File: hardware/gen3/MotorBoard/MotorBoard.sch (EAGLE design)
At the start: 249 parts, among them M10O1 TEST_PT, M1O2 TEST_PT, M1O3 TEST_PT, M2O1 TEST_PT, M2O2 TEST_PT, M2O3 TEST_PT, M3O1 TEST_PT, M3O2 TEST_PT, M3O3 TEST_PT, M4O1 TEST_PT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

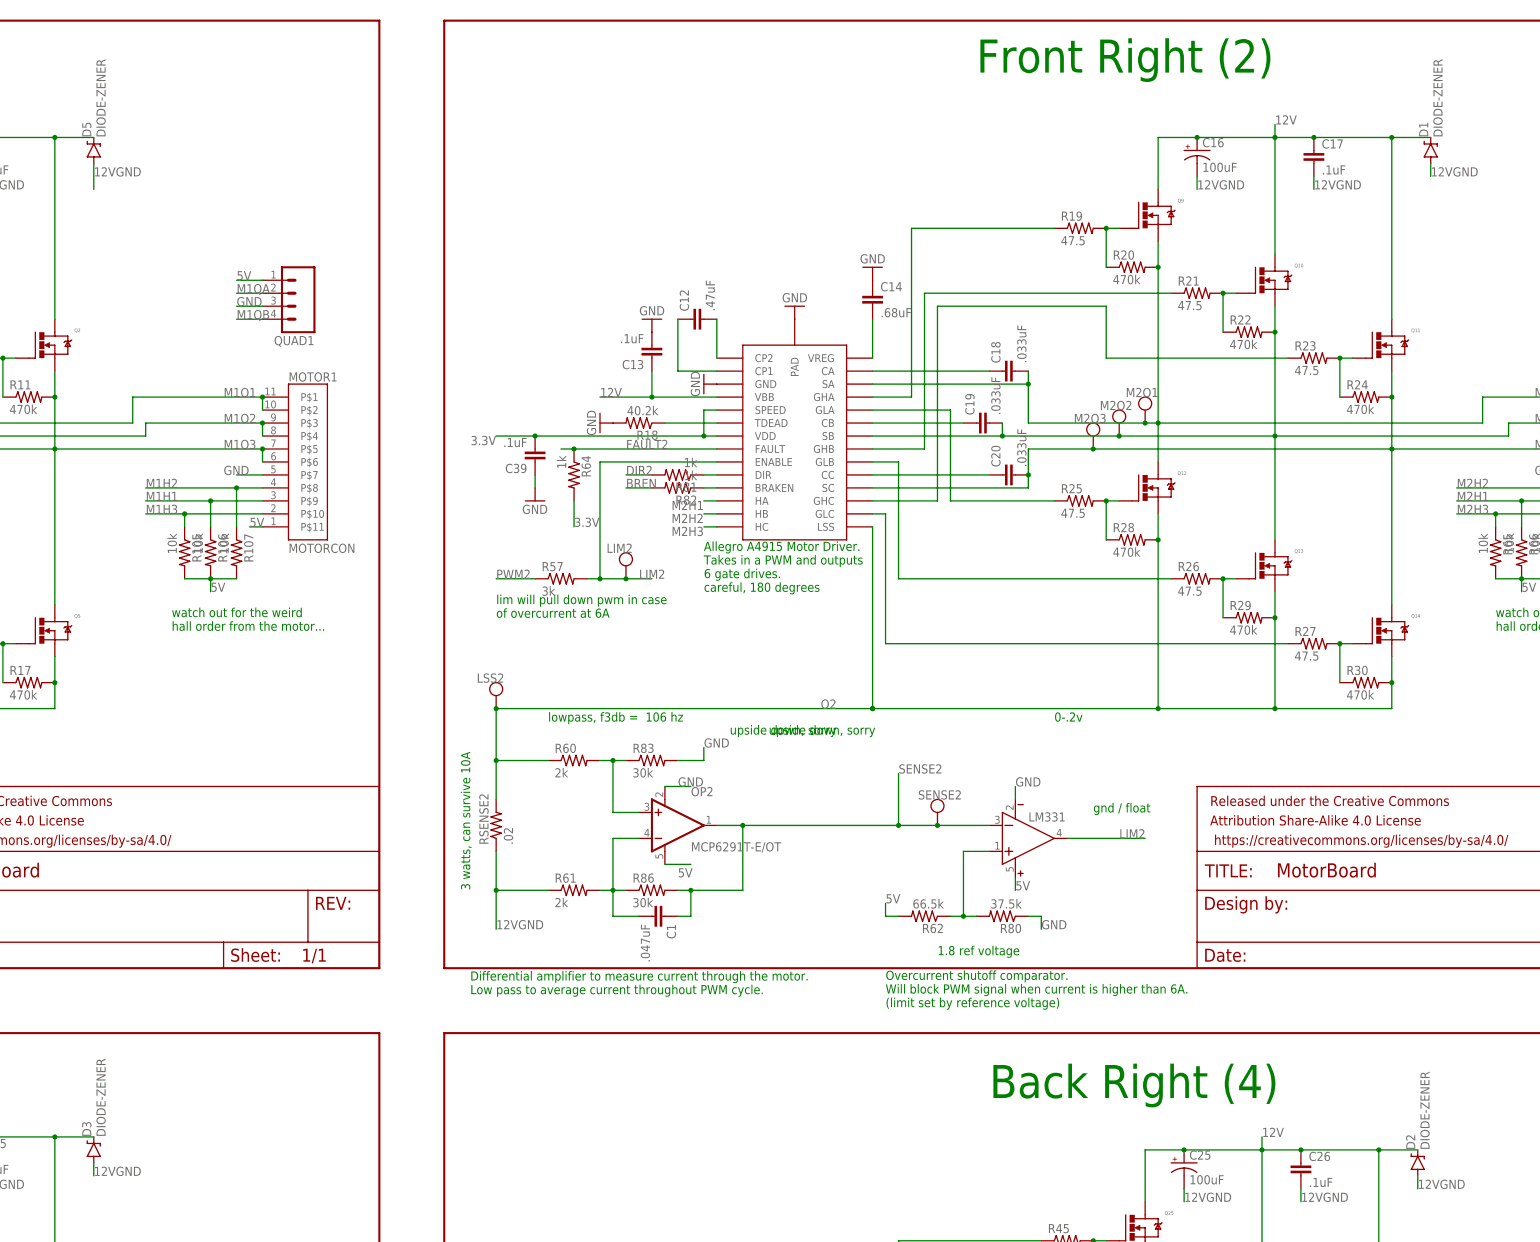
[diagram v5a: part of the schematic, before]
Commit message: smaller test pts
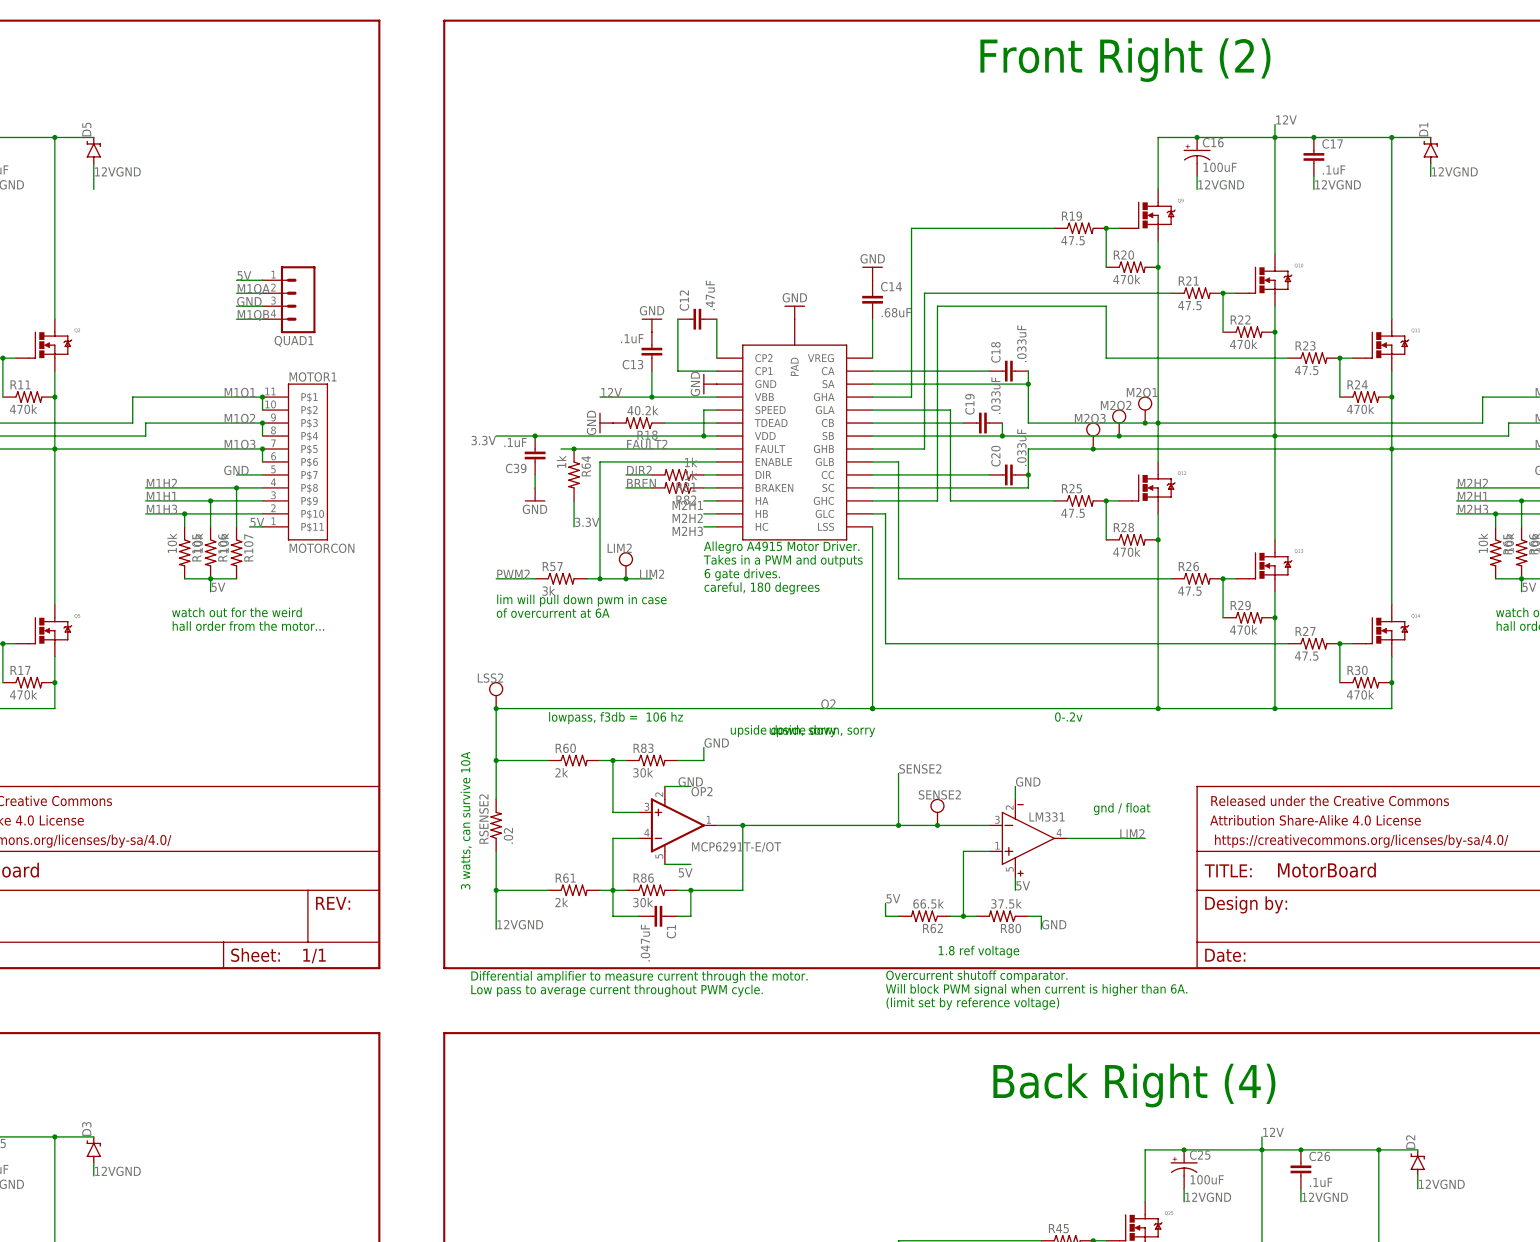
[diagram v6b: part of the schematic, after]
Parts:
- D1, D2, D3, D5: value DIODE-ZENER -> DIODE-ZENERDO214AB; device gen3:DIODE-ZENER -> gen3:DIODE-ZENERDO214AB
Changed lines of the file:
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@@
 <part name="C25" library="gen3" deviceset="CAP-POLAR" device="" value="100uF"/>
 <part name="C34" library="gen3" deviceset="CAP-POLAR" device="" value="100uF"/>
-<part name="D5" library="gen3" deviceset="DIODE-ZENER" device=""/>
-<part name="D1" library="gen3" deviceset="DIODE-ZENER" device=""/>
-<part name="D2" library="gen3" deviceset="DIODE-ZENER" device=""/>
-<part name="D3" library="gen3" deviceset="DIODE-ZENER" device=""/>
+<part name="D5" library="gen3" deviceset="DIODE-ZENER" device="DO214AB"/>
+<part name="D1" library="gen3" deviceset="DIODE-ZENER" device="DO214AB"/>
+<part name="D2" library="gen3" deviceset="DIODE-ZENER" device="DO214AB"/>
+<part name="D3" library="gen3" deviceset="DIODE-ZENER" device="DO214AB"/>
 <part name="JP1" library="SparkFun-Connectors" deviceset="M05X2" device="PTH"/>
 <part name="COMP1" library="gen3" deviceset="LM331" device=""/>

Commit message: temp sense and decoupling for motors
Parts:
- added C2, C41, C42, C50: 100uF, gen3:CAP-POLAR
- added C51, C52, C53, C54, C55, C56, C57, C58: .1uF, SparkFun-Passives:CAP0805
- added U$5, U$6, U$7, U$8: MCP9700SMD, SparkFun-Sensors:MCP9700SMD
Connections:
- new net TSENSE1: U$5.VO, U2.PF4
- new net TSENSE2: U$6.VO, U2.PF5
- new net TSENSE3: U$8.VO, U2.PF6
- new net TSENSE4: U$7.VO, U2.PF7
- net 12V: now also C2.+, C41.+, C42.+, C50.+
- net 12VGND: now also C2.-, C41.-, C42.-, C50.-
- net 3.3V: now also U$5.VCC, U$6.VCC, U$7.VCC, U$8.VCC
- net 5V: now also C51.2, C52.2, C53.2, C54.2, C55.2, C56.2, C57.2, C58.2
- net GND: now also C51.1, C52.1, C53.1, C54.1, C55.1, C56.1, C57.1, C58.1, U$5.GND, U$6.GND, U$7.GND, U$8.GND

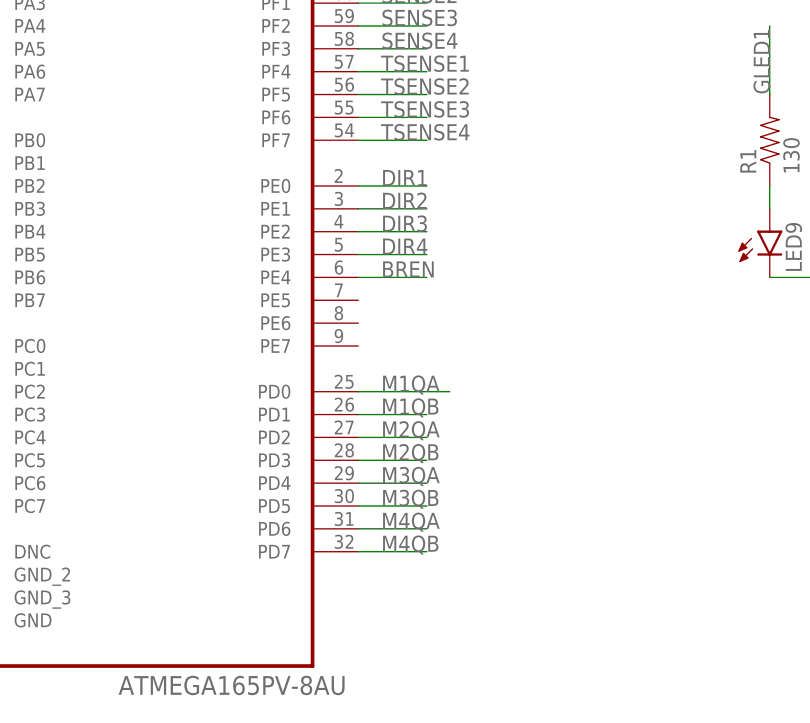
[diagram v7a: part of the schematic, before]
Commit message: Flipped ports d and e on motor board
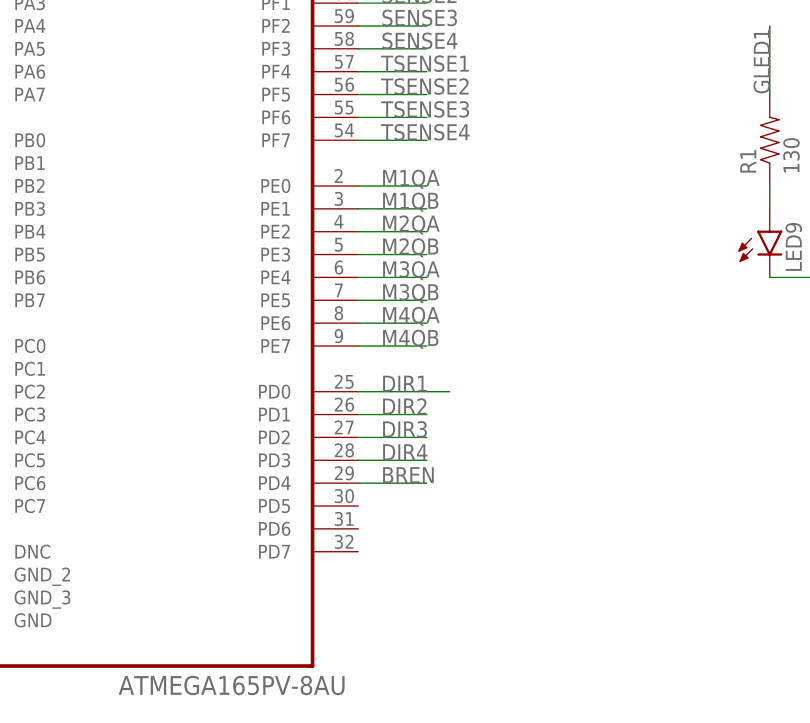
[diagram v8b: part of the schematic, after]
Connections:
- net BREN: now also U2.PD4; no longer U2.PE4
- net DIR1: now also U2.PD0; no longer U2.PE0
- net DIR2: now also U2.PD1; no longer U2.PE1
- net DIR3: now also U2.PD2; no longer U2.PE2
- net DIR4: now also U2.PD3; no longer U2.PE3
- net M1QA: now also U2.PE0; no longer U2.PD0
- net M1QB: now also U2.PE1; no longer U2.PD1
- net M2QA: now also U2.PE2; no longer U2.PD2
- net M2QB: now also U2.PE3; no longer U2.PD3
- net M3QA: now also U2.PE4; no longer U2.PD4
- net M3QB: now also U2.PE5; no longer U2.PD5
- net M4QA: now also U2.PE6; no longer U2.PD6
- net M4QB: now also U2.PE7; no longer U2.PD7
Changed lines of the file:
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@@
 <?xml version="1.0" encoding="utf-8"?>
 <!DOCTYPE eagle SYSTEM "eagle.dtd">
-<eagle version="6.4">
+<eagle version="7.2.0">
 <drawing>
 <settings>
@@
 <net name="M1QB" class="0">
 <segment>
-<pinref part="U2" gate="A" pin="PD1"/>
-<wire x1="144.78" y1="78.74" x2="152.4" y2="78.74" width="0.1524" layer="91"/>
-<label x="147.32" y="78.74" size="1.778" layer="95"/>
-</segment>
-<segment>
 <pinref part="QUAD1" gate="G$1" pin="4"/>
 <wire x1="490.22" y1="325.12" x2="485.14" y2="325.12" width="0.1524" layer="91"/>
 <label x="485.14" y="325.12" size="1.778" layer="95"/>
 </segment>
+<segment>
+<pinref part="U2" gate="A" pin="PE1"/>
+<wire x1="144.78" y1="101.6" x2="152.4" y2="101.6" width="0.1524" layer="91"/>
+<label x="147.32" y="101.6" size="1.778" layer="95"/>
+</segment>
 </net>
 <net name="M1QA" class="0">
-<segment>
-<pinref part="U2" gate="A" pin="PD0"/>
-<wire x1="144.78" y1="81.28" x2="154.94" y2="81.28" width="0.1524" layer="91"/>
-<label x="147.32" y="81.28" size="1.778" layer="95"/>
-</segment>
 <segment>
 <pinref part="QUAD1" gate="G$1" pin="2"/>
 <wire x1="490.22" y1="330.2" x2="485.14" y2="330.2" width="0.1524" layer="91"/>
 <label x="485.14" y="330.2" size="1.778" layer="95"/>
+</segment>
+<segment>
+<pinref part="U2" gate="A" pin="PE0"/>
+<wire x1="144.78" y1="104.14" x2="152.4" y2="104.14" width="0.1524" layer="91"/>
+<label x="147.32" y="104.14" size="1.778" layer="95"/>
 </segment>
 </net>
@@
 <net name="M2QA" class="0">
 <segment>
-<pinref part="U2" gate="A" pin="PD2"/>
-<wire x1="144.78" y1="76.2" x2="152.4" y2="76.2" width="0.1524" layer="91"/>
-<label x="147.32" y="76.2" size="1.778" layer="95"/>
-</segment>
-<segment>
 <pinref part="QUAD2" gate="G$1" pin="2"/>
 <wire x1="746.76" y1="330.2" x2="741.68" y2="330.2" width="0.1524" layer="91"/>
 <label x="741.68" y="330.2" size="1.778" layer="95"/>
 </segment>
+<segment>
+<pinref part="U2" gate="A" pin="PE2"/>
+<wire x1="144.78" y1="99.06" x2="152.4" y2="99.06" width="0.1524" layer="91"/>
+<label x="147.32" y="99.06" size="1.778" layer="95"/>
+</segment>
 </net>
 <net name="M2QB" class="0">
-<segment>
-<pinref part="U2" gate="A" pin="PD3"/>
-<wire x1="144.78" y1="73.66" x2="152.4" y2="73.66" width="0.1524" layer="91"/>
-<label x="147.32" y="73.66" size="1.778" layer="95"/>
-</segment>
 <segment>
 <pinref part="QUAD2" gate="G$1" pin="4"/>
@@
 <label x="741.68" y="325.12" size="1.778" layer="95"/>
 </segment>
+<segment>
+<pinref part="U2" gate="A" pin="PE3"/>
+<wire x1="144.78" y1="96.52" x2="152.4" y2="96.52" width="0.1524" layer="91"/>
+<label x="147.32" y="96.52" size="1.778" layer="95"/>
+</segment>
 </net>
 <net name="M3QA" class="0">
-<segment>
-<pinref part="U2" gate="A" pin="PD4"/>
-<wire x1="144.78" y1="71.12" x2="152.4" y2="71.12" width="0.1524" layer="91"/>
-<label x="147.32" y="71.12" size="1.778" layer="95"/>
-</segment>
 <segment>
 <pinref part="QUAD3" gate="G$1" pin="2"/>
@@
 <label x="480.06" y="134.62" size="1.778" layer="95"/>
 </segment>
+<segment>
+<pinref part="U2" gate="A" pin="PE4"/>
+<wire x1="144.78" y1="93.98" x2="152.4" y2="93.98" width="0.1524" layer="91"/>
+<label x="147.32" y="93.98" size="1.778" layer="95"/>
+</segment>
 </net>
 <net name="M3QB" class="0">
-<segment>
-<pinref part="U2" gate="A" pin="PD5"/>
-<wire x1="144.78" y1="68.58" x2="152.4" y2="68.58" width="0.1524" layer="91"/>
-<label x="147.32" y="68.58" size="1.778" layer="95"/>
-</segment>
 <segment>
 <pinref part="QUAD3" gate="G$1" pin="4"/>
@@
 <label x="480.06" y="129.54" size="1.778" layer="95"/>
 </segment>
+<segment>
+<pinref part="U2" gate="A" pin="PE5"/>
+<wire x1="144.78" y1="91.44" x2="152.4" y2="91.44" width="0.1524" layer="91"/>
+<label x="147.32" y="91.44" size="1.778" layer="95"/>
+</segment>
 </net>
 <net name="M4QA" class="0">
-<segment>
-<pinref part="U2" gate="A" pin="PD6"/>
-<wire x1="144.78" y1="66.04" x2="152.4" y2="66.04" width="0.1524" layer="91"/>
-<label x="147.32" y="66.04" size="1.778" layer="95"/>
-</segment>
 <segment>
 <pinref part="QUAD4" gate="G$1" pin="2"/>
@@
 <label x="741.68" y="132.08" size="1.778" layer="95"/>
 </segment>
+<segment>
+<pinref part="U2" gate="A" pin="PE6"/>
+<wire x1="144.78" y1="88.9" x2="152.4" y2="88.9" width="0.1524" layer="91"/>
+<label x="147.32" y="88.9" size="1.778" layer="95"/>
+</segment>
 </net>
 <net name="M4QB" class="0">
-<segment>
-<pinref part="U2" gate="A" pin="PD7"/>
-<wire x1="144.78" y1="63.5" x2="152.4" y2="63.5" width="0.1524" layer="91"/>
-<label x="147.32" y="63.5" size="1.778" layer="95"/>
-</segment>
 <segment>
 <pinref part="QUAD4" gate="G$1" pin="4"/>
 <wire x1="746.76" y1="127" x2="741.68" y2="127" width="0.1524" layer="91"/>
 <label x="741.68" y="127" size="1.778" layer="95"/>
+</segment>
+<segment>
+<pinref part="U2" gate="A" pin="PE7"/>
+<wire x1="144.78" y1="86.36" x2="152.4" y2="86.36" width="0.1524" layer="91"/>
+<label x="147.32" y="86.36" size="1.778" layer="95"/>
 </segment>
 </net>
@@
 </segment>
 <segment>
-<pinref part="U2" gate="A" pin="PE0"/>
-<wire x1="144.78" y1="104.14" x2="152.4" y2="104.14" width="0.1524" layer="91"/>
-<label x="147.32" y="104.14" size="1.778" layer="95"/>
+<pinref part="U2" gate="A" pin="PD0"/>
+<wire x1="144.78" y1="81.28" x2="154.94" y2="81.28" width="0.1524" layer="91"/>
+<label x="147.32" y="81.28" size="1.778" layer="95"/>
 </segment>
 </net>
@@
 </segment>
 <segment>
-<pinref part="U2" gate="A" pin="PE1"/>
-<wire x1="144.78" y1="101.6" x2="152.4" y2="101.6" width="0.1524" layer="91"/>
-<label x="147.32" y="101.6" size="1.778" layer="95"/>
+<pinref part="U2" gate="A" pin="PD1"/>
+<wire x1="144.78" y1="78.74" x2="152.4" y2="78.74" width="0.1524" layer="91"/>
+<label x="147.32" y="78.74" size="1.778" layer="95"/>
 </segment>
 </net>
@@
 </segment>
 <segment>
-<pinref part="U2" gate="A" pin="PE2"/>
-<wire x1="144.78" y1="99.06" x2="152.4" y2="99.06" width="0.1524" layer="91"/>
-<label x="147.32" y="99.06" size="1.778" layer="95"/>
+<pinref part="U2" gate="A" pin="PD2"/>
+<wire x1="144.78" y1="76.2" x2="152.4" y2="76.2" width="0.1524" layer="91"/>
+<label x="147.32" y="76.2" size="1.778" layer="95"/>
 </segment>
 </net>
@@
 </segment>
 <segment>
-<pinref part="U2" gate="A" pin="PE3"/>
-<wire x1="144.78" y1="96.52" x2="152.4" y2="96.52" width="0.1524" layer="91"/>
-<label x="147.32" y="96.52" size="1.778" layer="95"/>
+<pinref part="U2" gate="A" pin="PD3"/>
+<wire x1="144.78" y1="73.66" x2="152.4" y2="73.66" width="0.1524" layer="91"/>
+<label x="147.32" y="73.66" size="1.778" layer="95"/>
 </segment>
 </net>
@@
 </segment>
 <segment>
-<pinref part="U2" gate="A" pin="PE4"/>
-<wire x1="144.78" y1="93.98" x2="152.4" y2="93.98" width="0.1524" layer="91"/>
-<label x="147.32" y="93.98" size="1.778" layer="95"/>
-</segment>
-</net>
+<pinref part="U2" gate="A" pin="PD4"/>
+<wire x1="144.78" y1="71.12" x2="152.4" y2="71.12" width="0.1524" layer="91"/>
+<label x="147.32" y="71.12" size="1.778" layer="95"/>
+</segment>
+</net>
